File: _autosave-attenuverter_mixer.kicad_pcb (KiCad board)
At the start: 2 copper layers, 98 parts, among them J0 Eurorack power, J1 Input, J10 Or out, J2 Out, J3 Input, J4 Out, J5 Input, J6 Input, J7 Out, J8 Out, J9 Sum out, U1 TL072, U2 TL072, U3 TL072, U4 TL072, U5 TL074, U6 LM4040CIZ-5.0

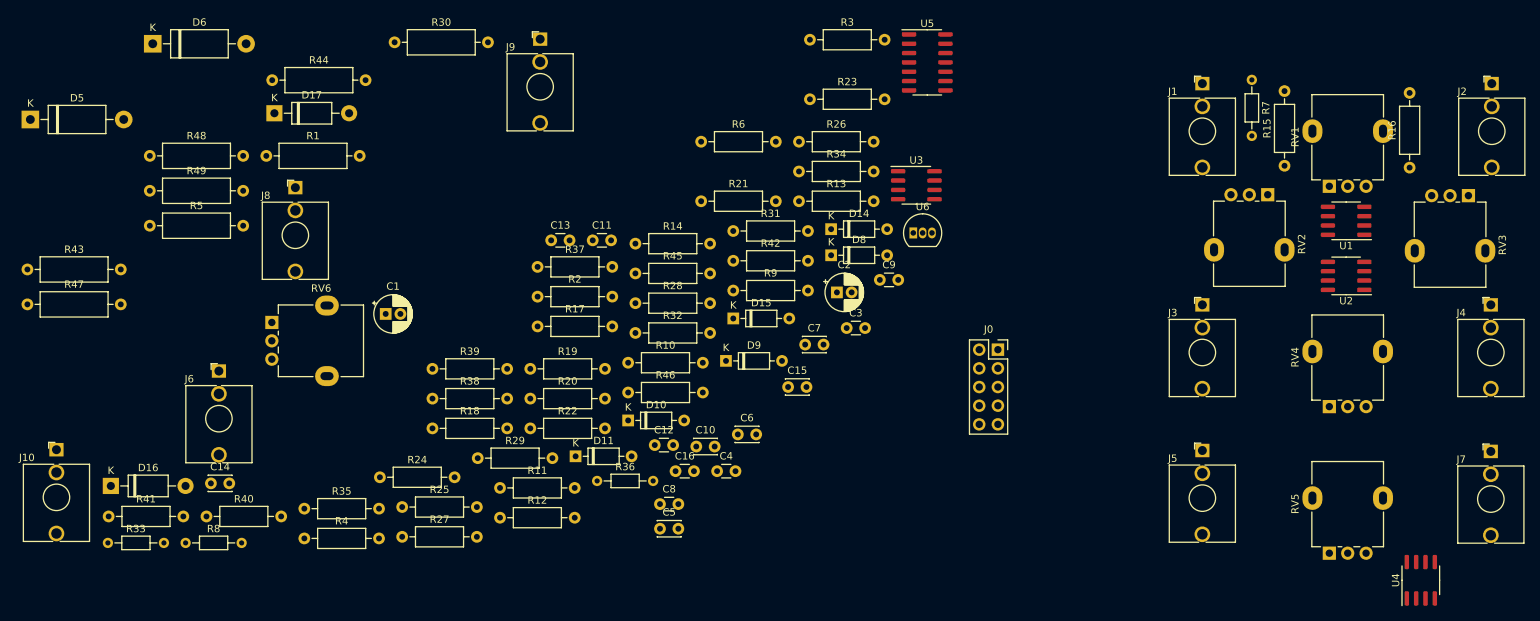
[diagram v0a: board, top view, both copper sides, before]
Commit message: remove two more TVS diodes; remove input resistors; use SM resistors
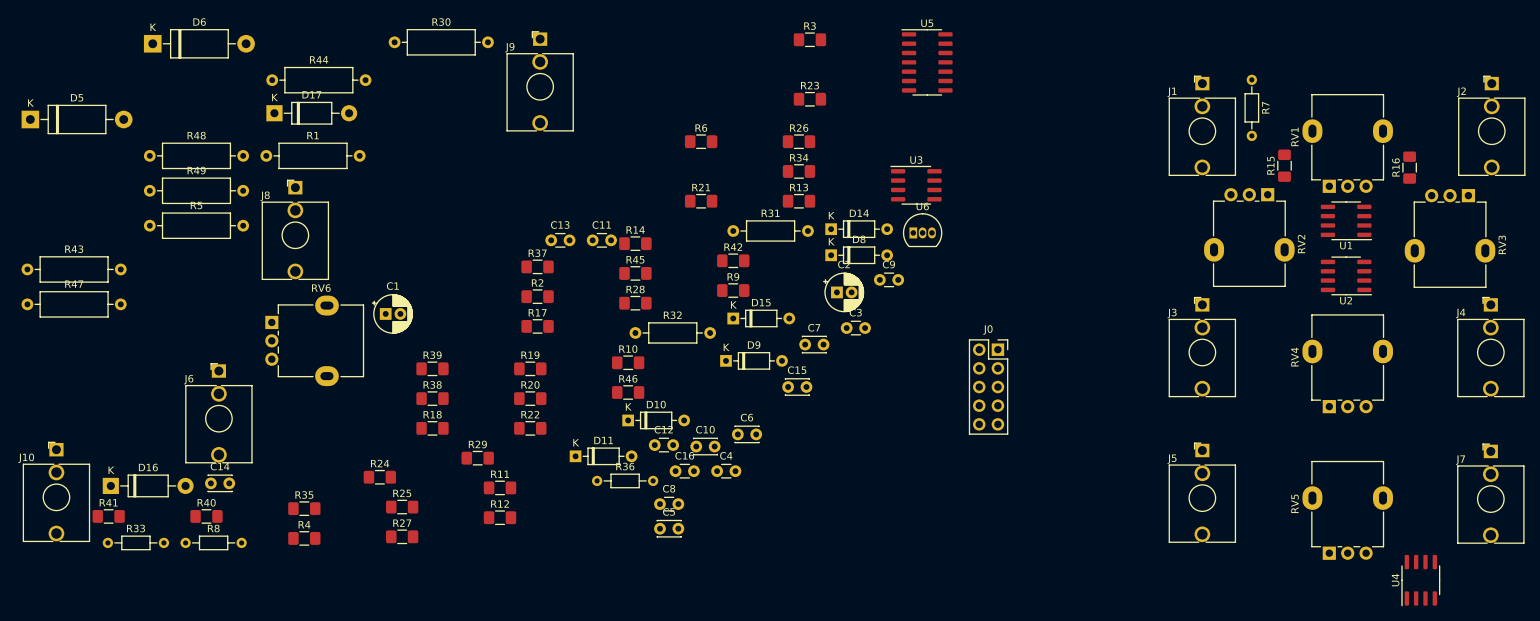
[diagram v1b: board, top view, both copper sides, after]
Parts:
- R10, R11, R12, R13, R14, R15, R16, R17, R18, R19, R2, R20, R21, R22, R23, R24, R25, R26, R27, R28, R29, R3, R34, R35, R37, R38, R39, R4, R40, R41, R42, R45, R46, R6, R9: footprint Resistor_THT:R_Axial_DIN0207_L6.3mm_D2.5mm_P10.16mm_Horizontal -> Resistor_SMD:R_1206_3216Metric_Pad1.42x1.75mm_HandSolder
